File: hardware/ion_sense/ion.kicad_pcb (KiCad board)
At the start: 2 copper layers, 37 parts, among them Q1 BC547, Q2 MPSA92, Q3 MPSA92, Q4 MPSA92, Q5 MPSA92, U1 LM2904, U2 LM7805

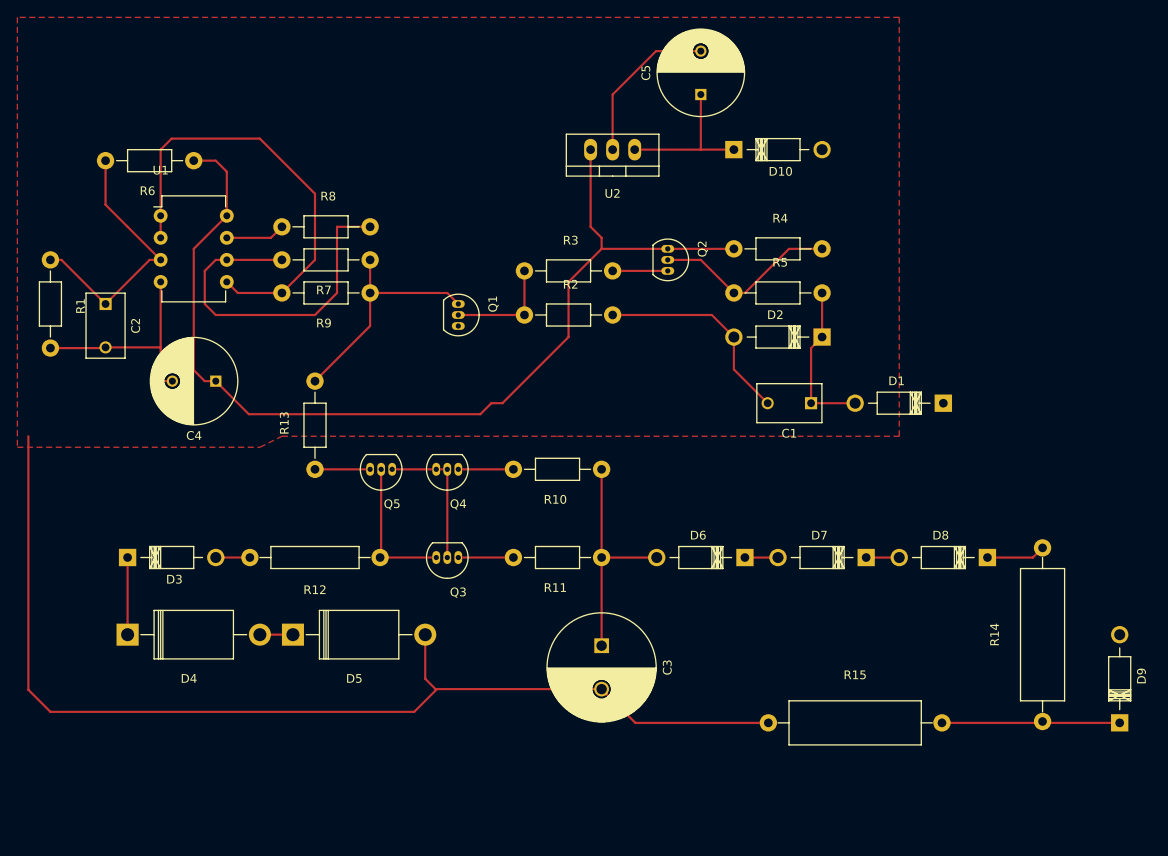
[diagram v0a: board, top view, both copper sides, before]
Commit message: 
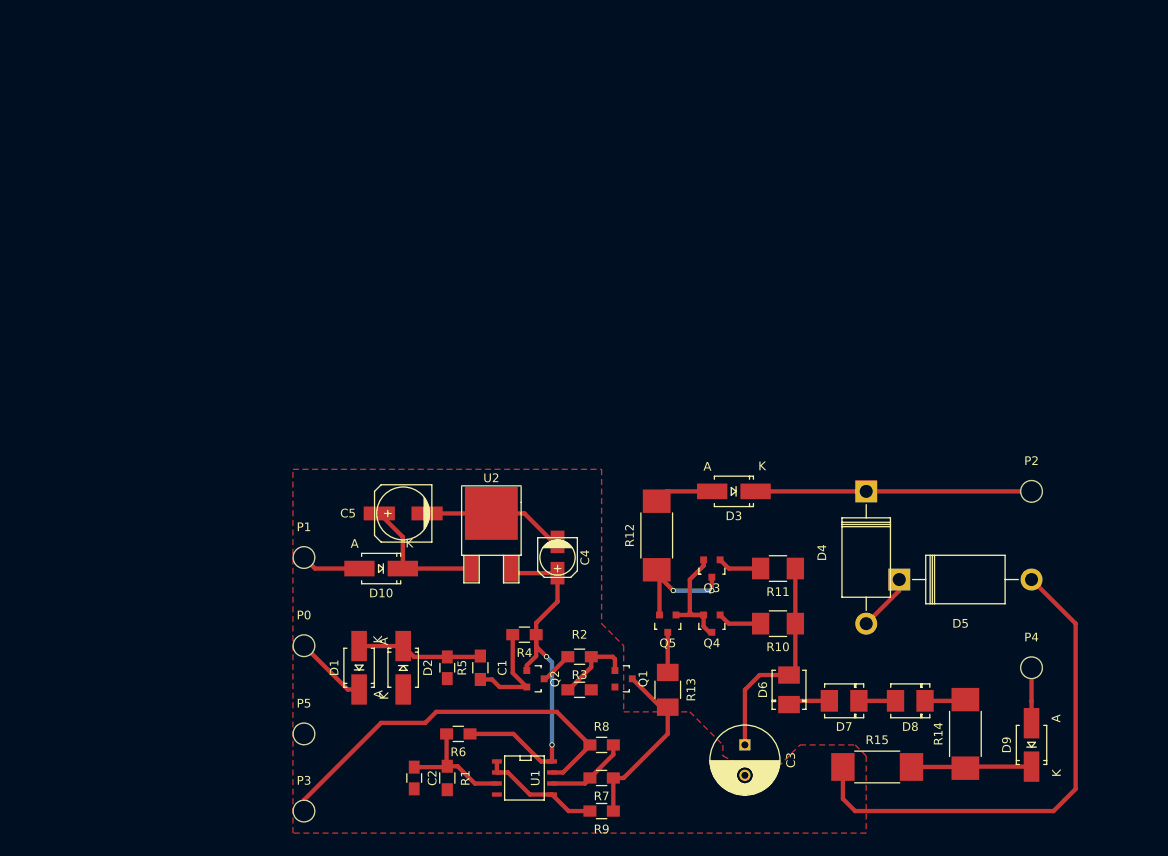
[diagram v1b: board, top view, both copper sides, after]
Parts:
- added P0: CONN_01X01, Mounting_Holes:MountingHole_2-5mm, F.Cu at (119.4, 118.1)
- added P1: CONN_01X01, Mounting_Holes:MountingHole_2-5mm, F.Cu at (119.4, 108.0)
- added P2: CONN_01X01, Mounting_Holes:MountingHole_2-5mm, F.Cu at (203.2, 100.3)
- added P3: CONN_01X01, Mounting_Holes:MountingHole_2-5mm, F.Cu at (119.4, 137.2)
- added P4: CONN_01X01, Mounting_Holes:MountingHole_2-5mm, F.Cu at (203.2, 120.7)
- added P5: CONN_01X01, Mounting_Holes:MountingHole_2-5mm, F.Cu at (119.4, 128.3)
- C1, C2: footprint Capacitors_ThroughHole:C_Disc_D7.5_P5 -> Capacitors_SMD:C_0805_HandSoldering
- C3: footprint Capacitors_ThroughHole:C_Radial_D12.5_L25_P5 -> Capacitors_ThroughHole:C_Radial_D8_L11.5_P3.5
- C4: footprint Capacitors_ThroughHole:C_Radial_D10_L25_P5 -> Capacitors_SMD:c_elec_4x4.5
- C5: footprint Capacitors_ThroughHole:C_Radial_D10_L25_P5 -> Capacitors_SMD:c_elec_6.3x4.5
- D1, D10, D2, D3, D9: value UF4007 -> US1M; footprint Diodes_ThroughHole:Diode_DO-41_SOD81_Horizontal_RM10 -> Diodes_SMD:SMA_Handsoldering
- D6, D7, D8: footprint Diodes_ThroughHole:Diode_DO-41_SOD81_Horizontal_RM10 -> Diodes_SMD:DO-214BA
- Q1: value BC547 -> MMBT3904; footprint TO_SOT_Packages_THT:TO-92_Inline_Narrow_Oval -> TO_SOT_Packages_SMD:SOT-23
- Q2, Q3, Q4, Q5: footprint TO_SOT_Packages_THT:TO-92_Inline_Narrow_Oval -> TO_SOT_Packages_SMD:SOT-23
- R1, R2, R3, R4, R5, R6, R7, R8, R9: footprint Resistors_ThroughHole:Resistor_Horizontal_RM10mm -> Resistors_SMD:R_0805_HandSoldering
- R10, R11, R13: footprint Resistors_ThroughHole:Resistor_Horizontal_RM10mm -> Resistors_SMD:R_1210_HandSoldering
- R12: footprint Resistors_ThroughHole:Resistor_Horizontal_RM15mm -> Resistors_SMD:R_2512_HandSoldering
- R14, R15: footprint Resistors_ThroughHole:Resistor_Horizontal_RM20mm -> Resistors_SMD:R_2512_HandSoldering
- U1: footprint Housings_DIP:DIP-8_W7.62mm -> SMD_Packages:SOIC-8-N
- U2: value LM7805 -> MC78M05CDT; footprint TO_SOT_Packages_THT:TO-220_Neutral123_Vertical -> TO_SOT_Packages_SMD:TO-252-2Lead
- moved D4 86.7 mm to (184.2, 100.3), turned to 270 degrees
- moved U1 77.1 mm to (144.8, 133.3), turned to 270 degrees
- moved R6 75.0 mm to (137.2, 128.3)
- moved D1 73.9 mm to (125.7, 120.7), turned to 90 degrees
- moved R1 71.2 mm to (135.9, 133.3)
- moved D3 70.3 mm to (168.9, 100.3), turned to 180 degrees
- moved D5 70.1 mm to (188.0, 110.5)
- moved R7 67.6 mm to (153.7, 133.3)
- moved R8 67.6 mm to (153.7, 129.5)
- moved R9 67.6 mm to (153.7, 137.2)
- moved C2 65.2 mm to (132.1, 133.3)
- moved D10 63.1 mm to (128.3, 109.2), turned to 180 degrees
- moved D2 61.5 mm to (130.8, 120.7), turned to 270 degrees
- moved C5 59.2 mm to (130.8, 102.9), turned to 180 degrees
- moved R5 55.1 mm to (139.7, 120.7), turned to 90 degrees
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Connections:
- net to_SoundCard renamed Net-(P3-Pad1)
- net to_coil_HV renamed Net-(D3-Pad1)
- C1 pad 2: GND -> Earth
- C2 pad 2: GND -> Earth
- C3 pad 2: GND -> Earth
- C4 pad 2: GND -> Earth
- C5 pad 2: GND -> Earth
- D1 pad 1: ignition_signal_from_ECU -> Net-(D1-Pad1)
- D10 pad 2: +12V -> Net-(D10-Pad2)
- D2 pad 2: GND -> Earth
- D5 pad 2: GND -> Earth
- D9 pad 2: +300V -> Net-(D9-Pad2)
- Q1 pad 2: Net-(Q1-Pad2) -> Earth
- Q1 pad 3: GND -> Net-(Q1-Pad3)
- R1 pad 2: GND -> Earth
- R13 pad 2: Net-(Q1-Pad1) -> Net-(Q1-Pad3)
- R15 pad 1: GND -> Earth
- R2 pad 1: Net-(Q1-Pad2) -> Net-(Q1-Pad1)
- R2 pad 2: GND -> Earth
- R3 pad 1: Net-(Q1-Pad2) -> Net-(Q1-Pad1)
- R7 pad 1: Net-(Q1-Pad1) -> Net-(Q1-Pad3)
- R9 pad 1: Net-(Q1-Pad1) -> Net-(Q1-Pad3)
- U1 pad 4: GND -> Earth
- U2 pad 1: (no net) -> Net-(C5-Pad1)
- U2 pad 2: (no net) -> Earth
- U2 pad 3: (no net) -> Net-(C4-Pad1)
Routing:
- net GND: track 193.5 -> 0.00 mm
- net Earth: track 0.00 -> 74.7 mm
- net Net-(C4-Pad1): track 116.7 -> 44.4 mm, vias 0 -> 2
- net Net-(P3-Pad1): track 6.88 -> 45.7 mm
- net Net-(R9-Pad2): track 51.0 -> 13.8 mm
- net Net-(R7-Pad2): track 41.5 -> 9.60 mm
- net Net-(D3-Pad1): track 8.89 -> 31.8 mm
- net Net-(Q1-Pad3): track 0.00 -> 20.7 mm
- net Net-(Q1-Pad1): track 27.3 -> 9.14 mm
- net Net-(C2-Pad1): track 31.0 -> 14.2 mm
- net Net-(Q1-Pad2): track 12.7 -> 0.00 mm
- net Net-(Q2-Pad2): track 21.5 -> 12.4 mm
- net Net-(D1-Pad1): track 0.00 -> 8.44 mm
- net Net-(D10-Pad2): track 0.00 -> 6.92 mm
- net Net-(D9-Pad1): track 20.6 -> 14.0 mm
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- added copper zone on F.Cu, net Earth
- removed copper zone on F.Cu, net GND
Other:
- net class 0.5: trace_width 0.5 -> 1
- net class Default: trace_width 0.25 -> 0.5

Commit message: newer version
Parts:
- removed D3: US1M, Diodes_SMD:SMA_Handsoldering
- removed D4, D5: 1.5KE200A, Diodes_ThroughHole:Diode_DO-201AD_Horizontal_RM15
- moved P2 34.3 mm to (168.9, 100.3)
- moved D9 29.6 mm to (188.0, 104.1), turned to 0 degrees
- moved R15 21.9 mm to (189.2, 110.5), turned to 180 degrees
- moved P4 17.3 mm to (198.1, 104.1)
- moved R14 13.1 mm to (189.2, 116.8), turned to 0 degrees
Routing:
- net Earth: track 74.7 -> 16.4 mm
- net Net-(D3-Pad1): track 31.8 -> 0.00 mm
- net Net-(D4-Pad2): track 6.66 -> 0.00 mm
- net Net-(D8-Pad1): track 4.71 -> 9.99 mm
- net Net-(D3-Pad2): track 6.86 -> 11.0 mm
- net Net-(D9-Pad2): track 6.39 -> 7.66 mm
- net Net-(D9-Pad1): track 14.0 -> 13.2 mm
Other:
- net class Default: trace_width 0.5 -> 1

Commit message: newer version
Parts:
- moved P4 10.2 mm to (188.0, 103.5)
- moved P3 8.03 mm to (121.9, 129.5)
- moved D1 6.84 mm to (128.3, 114.3), turned to 0 degrees
- moved R15 6.75 mm to (184.8, 115.6)
- moved P5 6.37 mm to (121.9, 122.4)
- moved D9 6.25 mm to (185.4, 109.9)
- moved R14 5.85 mm to (184.8, 120.7)
- moved D8 4.58 mm to (185.4, 127.0), turned to 270 degrees
- moved P0 4.58 mm to (121.9, 114.3)
- moved P1 4.58 mm to (121.9, 104.1)
- moved R9 3.81 mm to (153.7, 133.3)
- moved D7 2.84 mm to (180.3, 127.0), turned to 90 degrees
- moved R7 2.54 mm to (153.7, 130.8)
- moved P2 1.30 mm to (169.2, 101.6)
- moved R6 1.27 mm to (137.2, 127.0)
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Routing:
- net (no net): track 0.00 -> 8.13 mm
- net Net-(P3-Pad1): track 45.7 -> 39.5 mm
- net Net-(D1-Pad1): track 8.44 -> 3.85 mm
- net Net-(D8-Pad1): track 9.99 -> 7.22 mm
- net Net-(Q1-Pad3): track 20.7 -> 18.4 mm
- net Net-(C1-Pad1): track 14.5 -> 13.3 mm
- net Net-(R9-Pad2): track 13.8 -> 14.9 mm
- net Net-(D6-Pad1): track 4.83 -> 5.86 mm
- net Net-(D9-Pad2): track 7.66 -> 6.75 mm
- net Net-(D9-Pad1): track 13.2 -> 12.4 mm
- net Net-(D7-Pad1): track 4.22 -> 5.08 mm
- net Net-(R7-Pad2): track 9.60 -> 8.99 mm
- net Net-(C2-Pad1): track 14.2 -> 14.7 mm
- net Net-(C4-Pad1): track 44.4 -> 43.8 mm
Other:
- board text added: "+300V"
- board text added: "ION"
- board text added: "Ubat"
- board text added: "gnd"
- board text added: "ign"
- board text added: "to spark"
